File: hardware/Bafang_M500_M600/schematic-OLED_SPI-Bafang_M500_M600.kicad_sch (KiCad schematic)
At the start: 10 parts

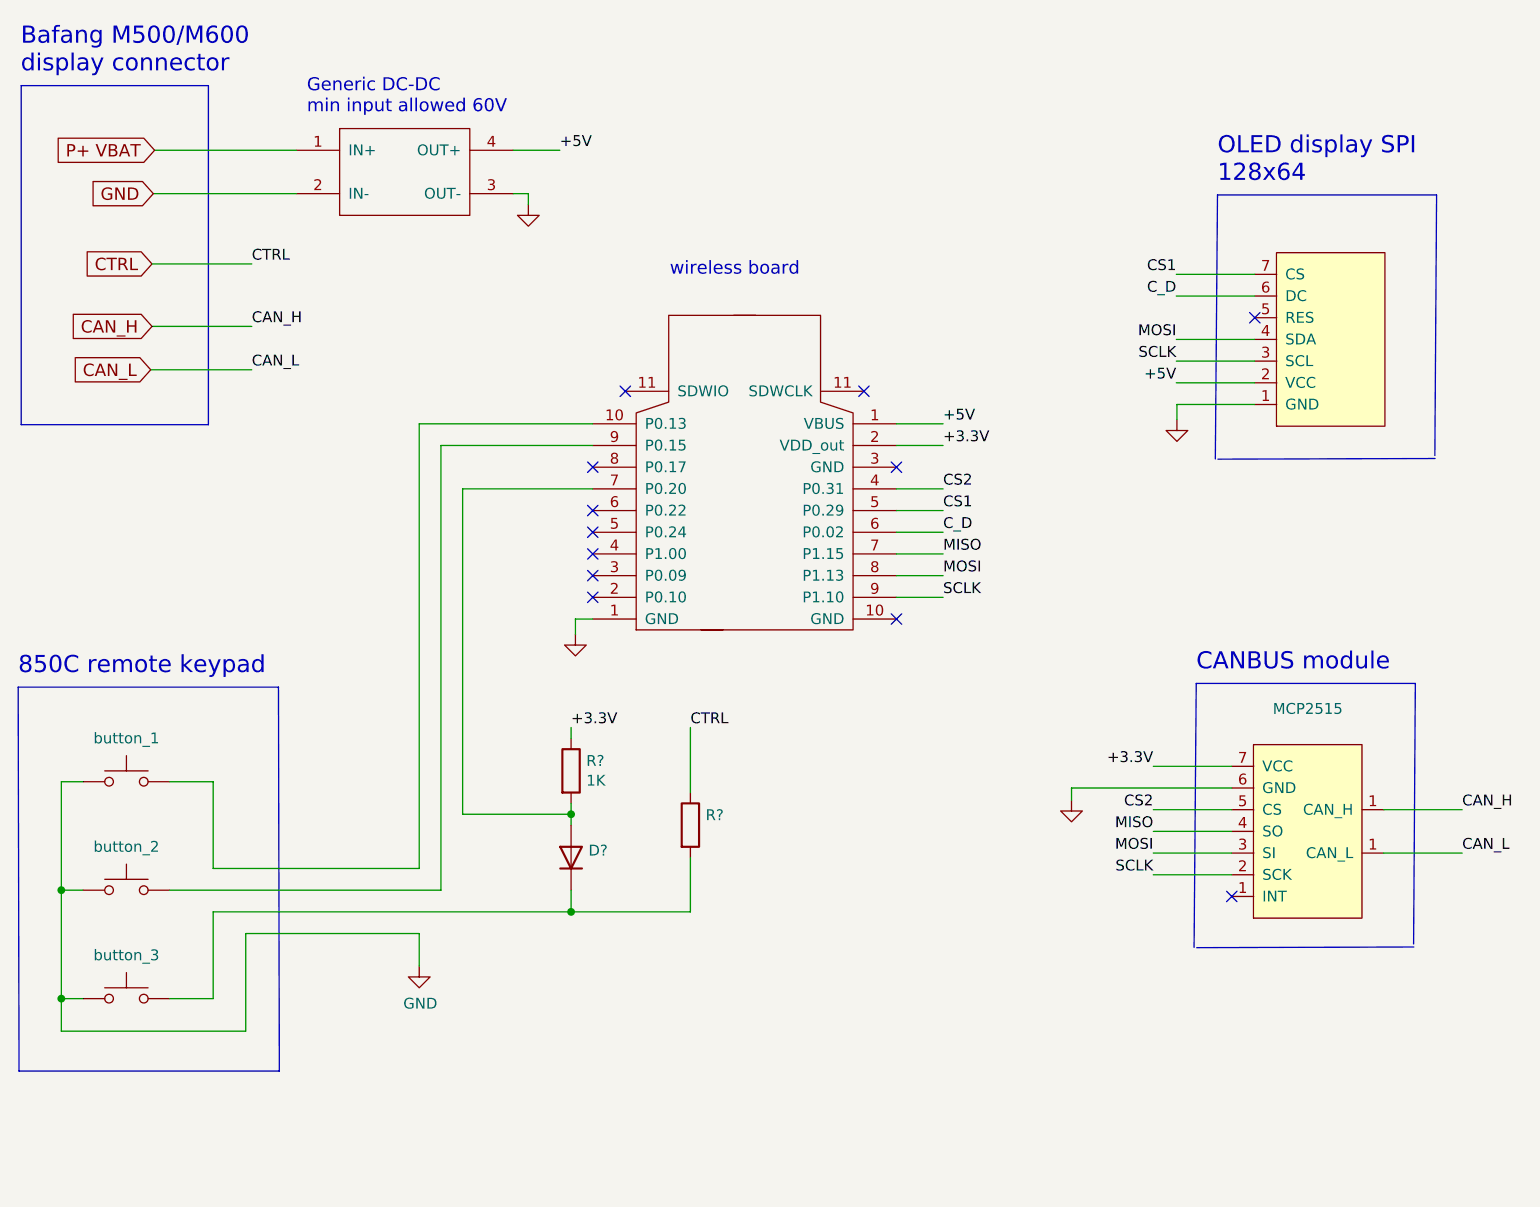
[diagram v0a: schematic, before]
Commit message: Schematic update to last working prototype
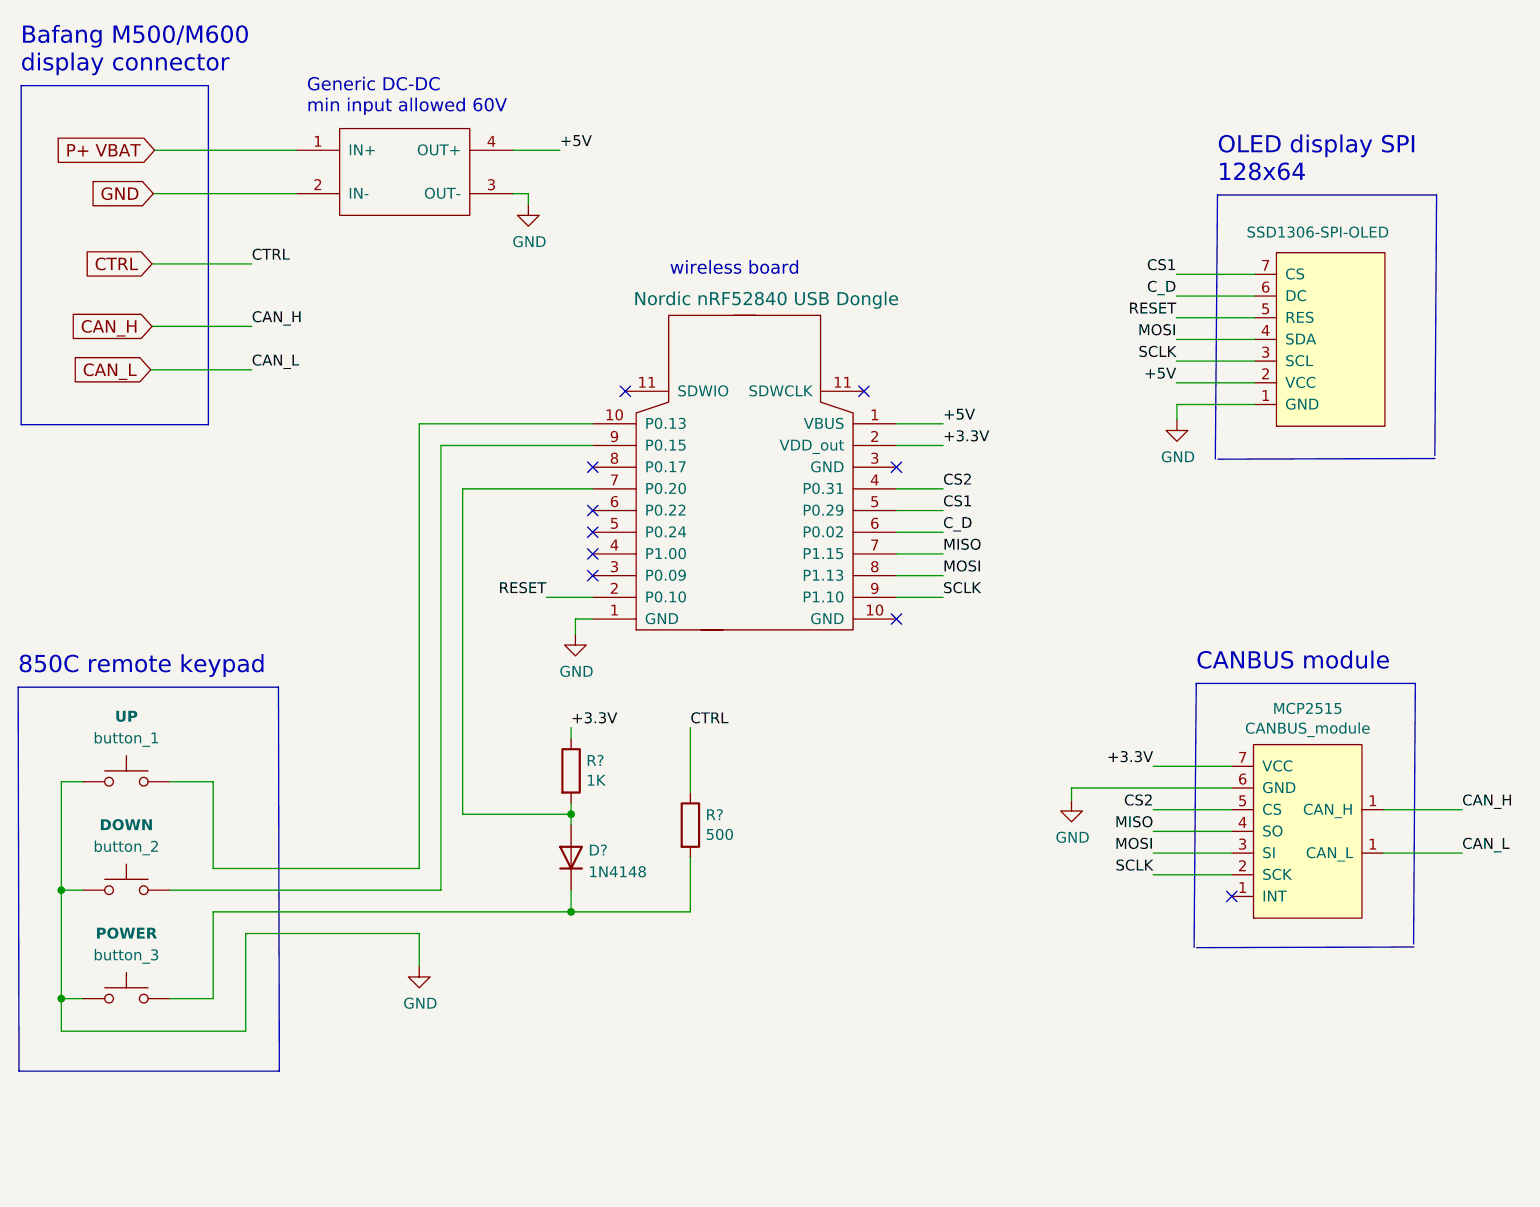
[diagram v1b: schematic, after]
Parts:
- D?: value (none) -> 1N4148; footprint (none) -> Diode_THT:D_DO-35_SOD27_P7.62mm_Horizontal
- MCP2515: value (none) -> CANBUS_module
- NA: value (none) -> SSD1306-SPI-OLED
- R?: value (none) -> 500
- U?: value (none) -> Nordic nRF52840 USB Dongle
- U?: value (none) -> Generic DC-DC (min input allowed 60V, output 5V)
- button_1: value (none) -> UP
- button_2: value (none) -> DOWN
- button_3: value (none) -> POWER
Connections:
- net RESET: now reaches U?.2 (VDD_out)
- net RESET: now also NA.5 (RES)
- no-connect marks 12 -> 10
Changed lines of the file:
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@@
   (no_connect (at 279.2984 175.9966))
   (no_connect (at 204.47 130.81))
-  (no_connect (at 204.47 140.97))
   (no_connect (at 208.28 116.84))
   (no_connect (at 240.03 125.73))
@@
   (no_connect (at 204.47 138.43))
   (no_connect (at 204.47 135.89))
-  (no_connect (at 281.9908 108.2294))
   (wire (pts (xy 215.9 156.21) (xy 215.9 163.83))
     (stroke (width 0) (type default) (color 0 0 0 0))
@@
     (stroke (width 0) (type default) (color 0 0 0 0))
   )
+  (wire (pts (xy 281.9908 108.2294) (xy 272.796 108.2294))
+    (stroke (width 0) (type default) (color 0 0 0 0))
+  )
   (wire (pts (xy 163.83 191.77) (xy 163.83 180.34))
     (stroke (width 0) (type default) (color 0 0 0 0))
@@
   )
   (wire (pts (xy 279.2984 173.4566) (xy 270.1036 173.4566))
+    (stroke (width 0) (type default) (color 0 0 0 0))
+  )
+  (wire (pts (xy 204.47 140.97) (xy 199.0344 140.97))
     (stroke (width 0) (type default) (color 0 0 0 0))
   )
@@
     (effects (font (size 1.27 1.27)) (justify left bottom))
   )
+  (label "RESET" (at 199.0344 140.97 180)
+    (effects (font (size 1.27 1.27)) (justify right bottom))
+  )
   (label "+3.3V" (at 270.1036 160.7566 180)
     (effects (font (size 1.27 1.27)) (justify right bottom))
@@
   )
   (label "SCLK" (at 272.796 113.3094 180)
+    (effects (font (size 1.27 1.27)) (justify right bottom))
+  )
+  (label "RESET" (at 272.796 108.2294 180)
     (effects (font (size 1.27 1.27)) (justify right bottom))
   )
@@
     (in_bom yes) (on_board yes)
     (property "Reference" "button_1" (id 0) (at 149.86 157.48 0))
-    (property "Value" "" (id 1) (at 149.86 154.94 0)
+    (property "Value" "UP" (id 1) (at 149.86 154.94 0)
       (effects (font (size 1.27 1.27) bold))
     )
@@
     (in_bom yes) (on_board yes)
     (property "Reference" "button_2" (id 0) (at 149.86 170.18 0))
-    (property "Value" "" (id 1) (at 149.86 167.64 0)
+    (property "Value" "DOWN" (id 1) (at 149.86 167.64 0)
       (effects (font (size 1.27 1.27) bold))
     )
@@
     (in_bom yes) (on_board yes)
     (property "Reference" "button_3" (id 0) (at 149.86 182.88 0))
-    (property "Value" "" (id 1) (at 149.86 180.34 0)
+    (property "Value" "POWER" (id 1) (at 149.86 180.34 0)
       (effects (font (size 1.27 1.27) bold))
     )
@@
       (effects (font (size 1.524 1.524)) hide)
     )
-    (property "Value" "" (id 1) (at 224.79 106.045 0)
+    (property "Value" "Nordic nRF52840 USB Dongle" (id 1) (at 224.79 106.045 0)
       (effects (font (size 1.524 1.524)))
     )
@@
       (effects (font (size 1.524 1.524)) hide)
     )
-    (property "Value" "" (id 1) (at 181.1782 83.5406 0)
+    (property "Value" "Generic DC-DC (min input allowed 60V, output 5V)" (id 1) (at 181.1782 83.5406 0)
       (effects (font (size 1.524 1.524)) hide)
     )
@@
       (effects (font (size 1.27 1.27)) hide)
     )
-    (property "Value" "" (id 1) (at 272.9992 124.5616 0))
+    (property "Value" "GND" (id 1) (at 272.9992 124.5616 0))
     (property "Footprint" "" (id 2) (at 272.8722 120.1674 0)
       (effects (font (size 1.27 1.27)) hide)
@@
       (effects (font (size 1.27 1.27)) hide)
     )
-    (property "Value" "" (id 1) (at 202.565 149.6822 0))
+    (property "Value" "GND" (id 1) (at 202.565 149.6822 0))
     (property "Footprint" "" (id 2) (at 202.438 145.288 0)
       (effects (font (size 1.27 1.27)) hide)
@@
       (effects (font (size 1.27 1.27)) hide)
     )
-    (property "Value" "" (id 1) (at 197.0532 99.3648 0))
+    (property "Value" "GND" (id 1) (at 197.0532 99.3648 0))
     (property "Footprint" "" (id 2) (at 196.9262 94.9706 0)
       (effects (font (size 1.27 1.27)) hide)
@@
       (effects (font (size 1.27 1.27)) (justify right) hide)
     )
-    (property "Value" "" (id 1) (at 281.0256 98.2472 90)
+    (property "Value" "SSD1306-SPI-OLED" (id 1) (at 281.0256 98.2472 90)
       (effects (font (size 1.27 1.27)) (justify right))
     )
@@
     (in_bom yes) (on_board yes)
     (property "Reference" "MCP2515" (id 0) (at 288.1884 154.0256 90))
-    (property "Value" "" (id 1) (at 288.1884 156.337 90))
+    (property "Value" "CANBUS_module" (id 1) (at 288.1884 156.337 90))
     (property "Footprint" "" (id 2) (at 281.8384 172.1866 0)
       (effects (font (size 1.27 1.27)) hide)
@@
       (effects (font (size 1.27 1.27)) hide)
     )
-    (property "Value" "" (id 1) (at 260.6548 169.1132 0))
+    (property "Value" "GND" (id 1) (at 260.6548 169.1132 0))
     (property "Footprint" "" (id 2) (at 260.5278 164.719 0)
       (effects (font (size 1.27 1.27)) hide)
@@
       (effects (font (size 1.27 1.27)) (justify right))
     )
-    (property "Value" "" (id 1) (at 203.962 173.1522 90)
+    (property "Value" "1N4148" (id 1) (at 203.962 173.1522 90)
       (effects (font (size 1.27 1.27)) (justify right))
     )
-    (property "Footprint" "" (id 2) (at 206.375 171.45 0)
+    (property "Footprint" "Diode_THT:D_DO-35_SOD27_P7.62mm_Horizontal" (id 2) (at 206.375 171.45 0)
       (effects (font (size 1.27 1.27)) hide)
     )
@@
       (effects (font (size 1.27 1.27)) (justify left))
     )
-    (property "Value" "" (id 1) (at 217.678 168.783 0)
+    (property "Value" "500" (id 1) (at 217.678 168.783 0)
       (effects (font (size 1.27 1.27)) (justify left))
     )

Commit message: Updated firmware for Bafang version, now on_off button works. Updated the schematic based on current prototype
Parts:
- removed U?: Generic DC-DC (min input allowed 60V, output 5V), symbol schematic-OLED_SPI-Bafang_M500_M600-rescue:Generic_DC-DC-Wireless_eBike-Wireles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
- added U?: STH0548S05, symbol schematic-OLED_SPI-Bafang_M500_M600-rescue:DC-DC
- R1: renamed from R?; value 500 -> 470R
- R2: renamed from R?; value 1K -> 3K3
- gave numbers to parts that had none: 2
- renumbered NA to NA1
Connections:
- net +5V: now also U?.5 (OUT+)
- net CS2: now also U2.3 (P0.09); no longer U2.4 (P1.00)
- net GND: now also U?.7 (OUT-), U?.9 (IN-)
- net P+ VBAT: now also U?.1 (IN+)
- net ON_OFF_BUTTON: now reaches U2.4 (P1.00)
- net ON_OFF_BUTTON: now also D1.2 (A), R2.2
- no-connect marks 10 -> 12
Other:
- note added: "DC-DC converter Battery voltage to 5V"
- note removed: "Generic DC-DC min input allowed 60V"
- moved on the sheet: D1, R1, R2

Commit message: Updated the schematic - walk assist works. Updated the firmware for latest hardware
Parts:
- added D2: 1N4148, Diode_THT:D_DO-35_SOD27_P7.62mm_Horizontal, symbol Diode:1N4148
- added R3: 3K3, symbol Device:R
- added R4: 1K5, symbol Device:R
- gave numbers to parts that had none: 1
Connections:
- net +3.3V: now also R3.1
- net CS2: now also U2.4 (P1.00); no longer U2.3 (P0.09)
- net CTRL: now also R4.1
- net at button_2.2: now also D2.1 (K), R4.2; no longer U2.9 (P1.10)
- net ON_OFF_BUTTON: no longer names the net of D1.2 (A), R2.2
- net ON_OFF_BUTTON: now also U2.7 (P1.15); no longer U2.4 (P1.00)
- new net: D2.2 (A), R3.2, U2.9 (P1.10)
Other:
- moved on the sheet: D1, R1, R2, button_1, button_2, button_3
